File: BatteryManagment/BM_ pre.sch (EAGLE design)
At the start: 123 parts, among them IC1 LMV321M5, U1 ATMEGA328P-AU, U2 LTC4440EMS8E-5PBF

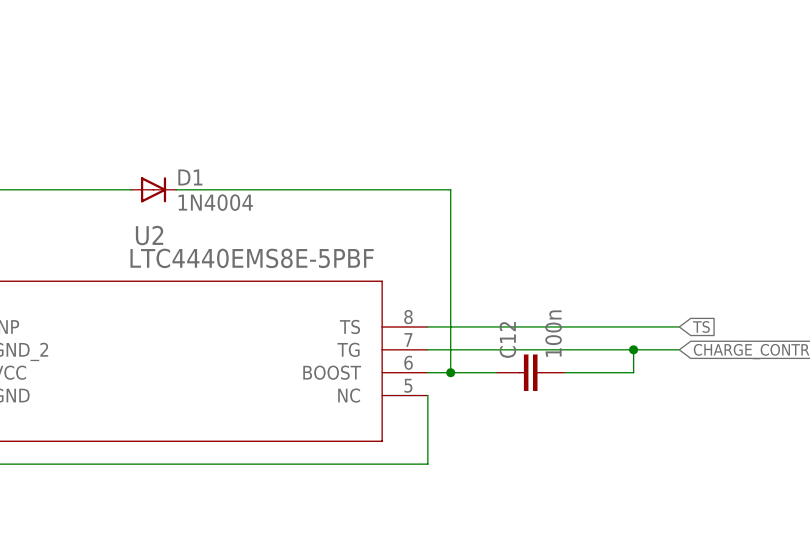
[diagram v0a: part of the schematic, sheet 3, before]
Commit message: Revert "Finished version v0.2"
This reverts commit a5989fd47d9f9b1588f2c3c09283aac7458017f8.
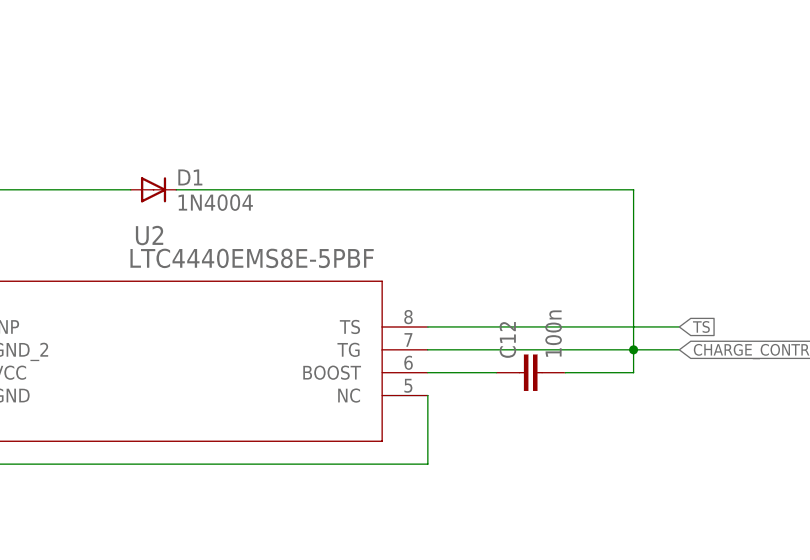
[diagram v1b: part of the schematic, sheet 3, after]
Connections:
- net CHARGE_CONTROL: now also D1.C
- net N$2: no longer D1.C
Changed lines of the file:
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@@
+</segment>
+</net>
+<net name="CHARGE_CONTROL" class="0">
+<segment>
+<pinref part="U2" gate="A" pin="TG"/>
+<wire x1="284.48" y1="60.96" x2="307.34" y2="60.96" width="0.1524" layer="91"/>
+<label x="312.42" y="60.96" size="1.27" layer="95" xref="yes"/>
+<pinref part="C12" gate="G$1" pin="2"/>
+<wire x1="307.34" y1="60.96" x2="312.42" y2="60.96" width="0.1524" layer="91"/>
+<wire x1="299.72" y1="58.42" x2="307.34" y2="58.42" width="0.1524" layer="91"/>
+<wire x1="307.34" y1="58.42" x2="307.34" y2="60.96" width="0.1524" layer="91"/>
+<junction x="307.34" y="60.96"/>
+<pinref part="D1" gate="1" pin="C"/>
+<wire x1="256.54" y1="78.74" x2="307.34" y2="78.74" width="0.1524" layer="91"/>
+<wire x1="307.34" y1="78.74" x2="307.34" y2="60.96" width="0.1524" layer="91"/>
 </segment>
 </net>
@@
 <pinref part="C12" gate="G$1" pin="1"/>
 <pinref part="U2" gate="A" pin="BOOST"/>
-<wire x1="292.1" y1="58.42" x2="287.02" y2="58.42" width="0.1524" layer="91"/>
-<pinref part="D1" gate="1" pin="C"/>
-<wire x1="287.02" y1="58.42" x2="284.48" y2="58.42" width="0.1524" layer="91"/>
-<wire x1="256.54" y1="78.74" x2="287.02" y2="78.74" width="0.1524" layer="91"/>
-<wire x1="287.02" y1="78.74" x2="287.02" y2="58.42" width="0.1524" layer="91"/>
-<junction x="287.02" y="58.42"/>
+<wire x1="292.1" y1="58.42" x2="284.48" y2="58.42" width="0.1524" layer="91"/>
 </segment>
 </net>
@@
 </segment>
 </net>
-<net name="CHARGE_CONTROL" class="0">
-<segment>
-<wire x1="307.34" y1="60.96" x2="312.42" y2="60.96" width="0.1524" layer="91"/>
-<pinref part="C12" gate="G$1" pin="2"/>
-<wire x1="299.72" y1="58.42" x2="307.34" y2="58.42" width="0.1524" layer="91"/>
-<wire x1="307.34" y1="58.42" x2="307.34" y2="60.96" width="0.1524" layer="91"/>
-<junction x="307.34" y="60.96"/>
-<pinref part="U2" gate="A" pin="TG"/>
-<wire x1="284.48" y1="60.96" x2="307.34" y2="60.96" width="0.1524" layer="91"/>
-<label x="312.42" y="60.96" size="1.27" layer="95" xref="yes"/>
-</segment>
-</net>
